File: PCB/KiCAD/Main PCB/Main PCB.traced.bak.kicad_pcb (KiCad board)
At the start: 2 copper layers, 118 x 118 mm, 130 parts, among them IC1 ADG608BRZ, IC2 ADG608BRZ, IC3 VNH7070ASTR, IC4 VNH7070ASTR, IC5 VNH7070ASTR, IC6 VNH7070ASTR, IC7 VNH7070ASTR, IC8 XB3-24Z8CM, J1 Conn_01x04, J10 Conn_01x02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

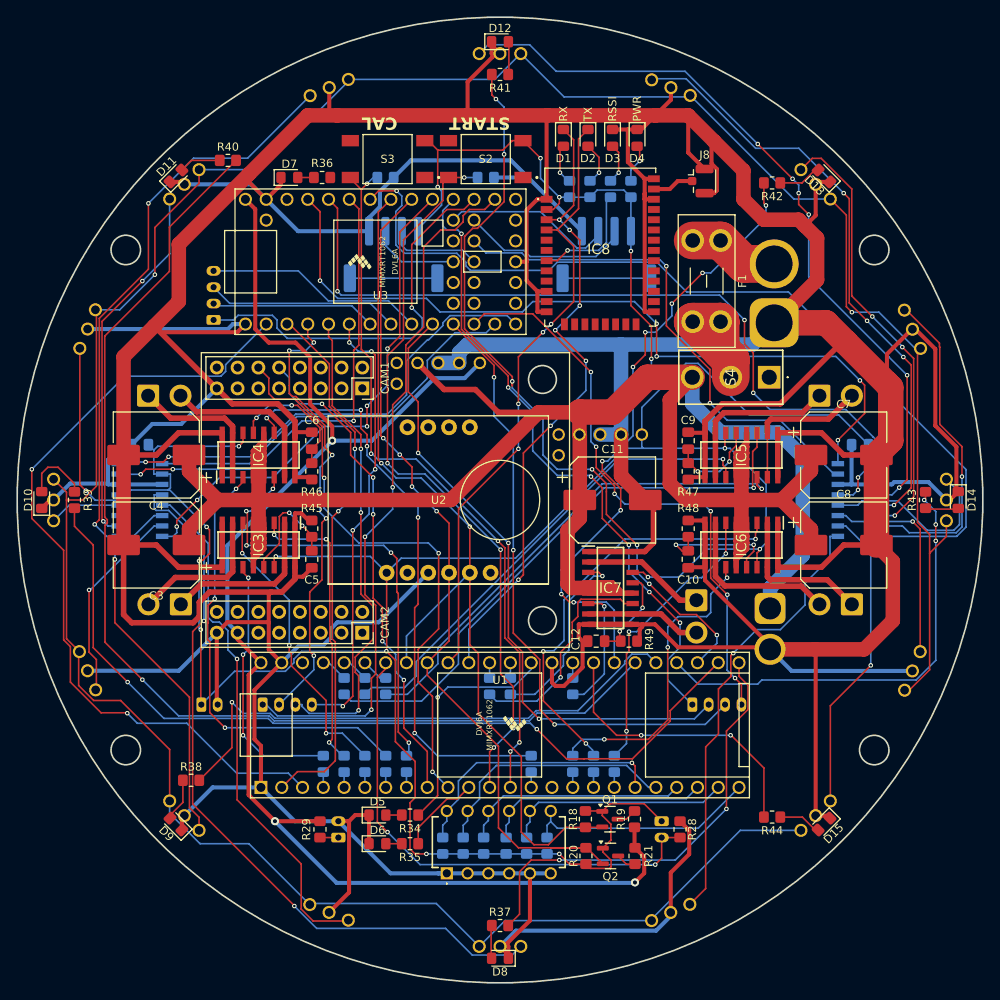
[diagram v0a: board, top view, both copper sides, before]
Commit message: Finished traces and made them curved
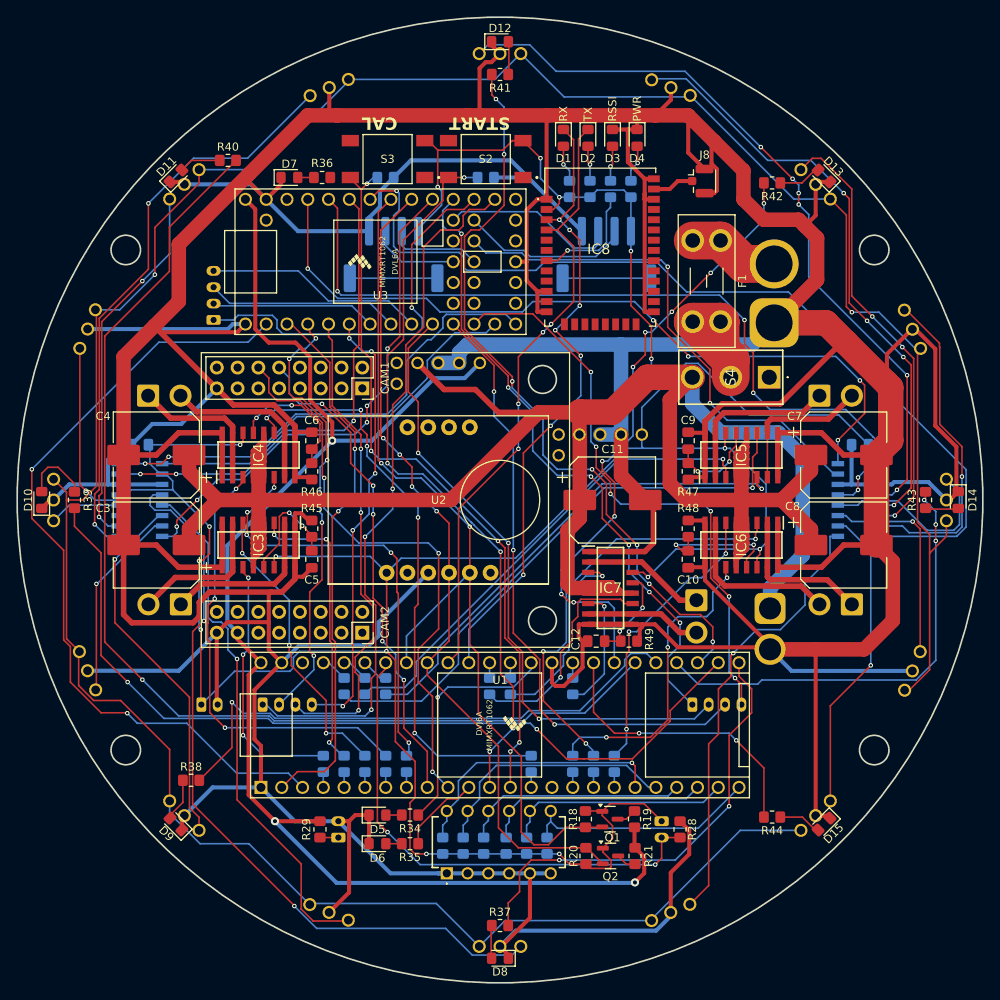
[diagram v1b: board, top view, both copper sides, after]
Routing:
- net 3V3_SDA: track 105.3 -> 101.0 mm
- net GND: track 1076.0 -> 1073.2 mm
- net TSSP_2_A1: track 96.7 -> 94.5 mm
- net IR_DIR_225: track 78.0 -> 76.4 mm
- net SPARE_SDA: track 20.6 -> 21.8 mm
- net LED_1_A0: track 55.4 -> 54.2 mm
- net IN_B_M2: track 53.6 -> 52.6 mm
- net Net-(D2-A): track 5.31 -> 4.36 mm
- net IN_A_M4: track 51.7 -> 52.6 mm
- net Net-(IC1-S4): track 24.7 -> 23.8 mm
- net TSSP_2_OUT: track 110.7 -> 111.4 mm
- net Net-(IC1-S1): track 91.0 -> 91.7 mm
- net TSSP_1_A1: track 59.2 -> 59.9 mm
- net IN_A_DRIB: track 23.4 -> 24.0 mm
- net Net-(D3-A): track 5.00 -> 4.45 mm
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
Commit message: Redone main PCB traces and started lower PCB
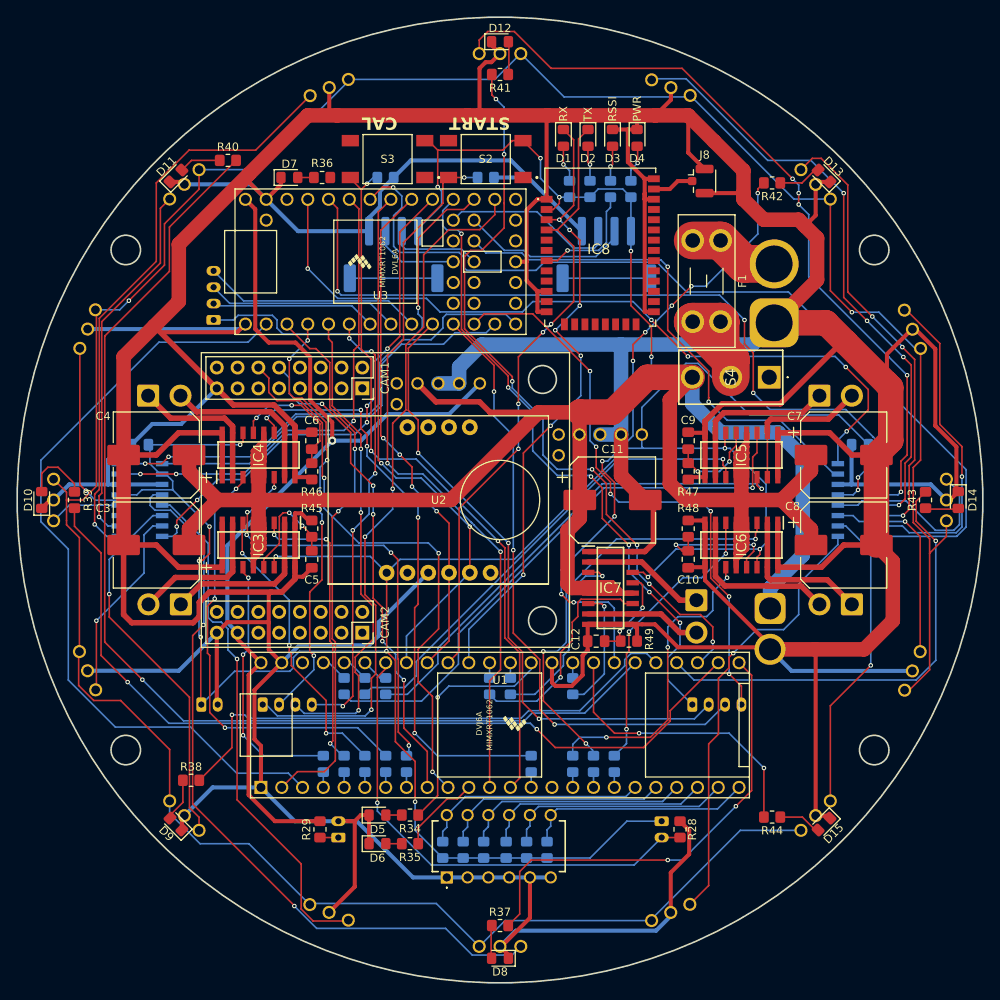
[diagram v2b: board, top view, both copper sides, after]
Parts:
- removed Q1, Q2: BSS138, Package_TO_SOT_SMD:SOT-23
- removed R18, R19, R20, R21: 10k, Resistor_SMD:R_0805_2012Metric_Pad1.20x1.40mm_HandSolder
- IR1, IR10, IR11, IR12, IR13, IR14, IR15, IR16, IR2, IR3, IR4, IR5, IR6, IR7, IR8, IR9: value TSSP4038 -> TSOP34840
- moved U5 2.50 mm to (-9.99, -5.12)
- moved R1 0.50 mm to (-7.00, 42.8)
- moved R10 0.50 mm to (0.75, 42.8)
- moved R11 0.50 mm to (3.25, 42.8)
- moved R16 0.50 mm to (5.75, 42.8)
- moved R2 0.50 mm to (-4.50, 42.8)
- moved R5 0.50 mm to (-2.00, 42.8)
- moved S1 0.50 mm to (-6.50, 46.1)
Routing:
- net +5V: track 173.5 -> 117.7 mm, vias 3 -> 1
- net 3V3_SCL: track 112.6 -> 66.9 mm
- net 3V3_SDA: track 101.0 -> 62.8 mm
- net +3V3: track 380.7 -> 367.3 mm, vias 18 -> 17
- net Net-(U1-27_A13_SCK1): track 33.0 -> 27.9 mm, vias 1 -> 0
- net GND: track 1073.2 -> 1069.8 mm
- net Net-(U1-28_RX7): track 31.1 -> 27.9 mm
- net Net-(IC2-S1): track 91.9 -> 94.6 mm, vias 6 -> 5
- net 5V_SDA: track 2.48 -> 0.00 mm
- net 5V_SCL: track 2.48 -> 0.00 mm
- net LG_RECEIVE: track 61.9 -> 59.7 mm, vias 2 -> 1
- net IR_DIR_45: track 68.0 -> 65.8 mm
- net TSSP_1_A0: track 49.0 -> 50.7 mm
- net START_BUTTON: track 90.4 -> 89.1 mm, vias 5 -> 3
- net LED_1_A0: track 54.2 -> 53.0 mm
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
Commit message: Started routing lower PCB
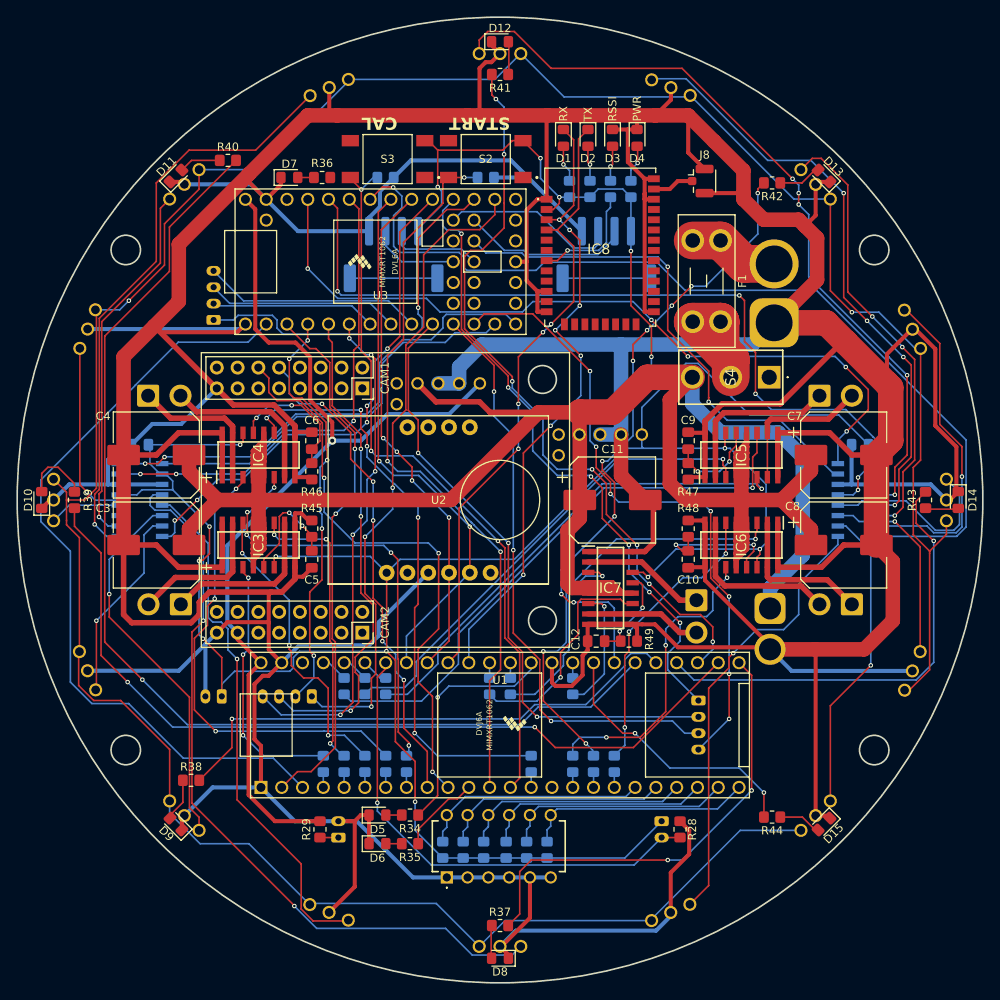
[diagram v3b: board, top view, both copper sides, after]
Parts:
- moved J1 6.08 mm to (-23.0, 24.0), turned to 180 degrees
- moved J10 2.69 mm to (-34.0, 24.0), turned to 180 degrees
- moved J3 0.90 mm to (24.2, 24.5), turned to -90 degrees
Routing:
- net LED_1_A2: track 54.2 -> 61.6 mm
- net LED_3_A2: track 71.9 -> 78.4 mm, vias 6 -> 7
- net LED_1_OUT: track 85.7 -> 79.3 mm
- net LED_3_A1: track 75.9 -> 72.1 mm
- net IR_DIR_315: track 35.7 -> 33.4 mm
- net IN_A_M2: track 53.8 -> 56.0 mm
- net TSSP_2_OUT: track 112.1 -> 114.2 mm
- net LED_3_A0: track 77.5 -> 75.5 mm
- net +3V3: track 367.3 -> 365.4 mm
- net LED_1_A0: track 53.0 -> 51.1 mm
- net GND: track 1069.8 -> 1068.2 mm
- net LED_1_A1: track 58.9 -> 60.5 mm
- net TEENSY_1_TX: track 96.7 -> 95.3 mm
- net TSSP_2_A0: track 92.8 -> 94.1 mm
- net IN_B_M1: track 35.9 -> 36.9 mm
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
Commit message: Added another switch
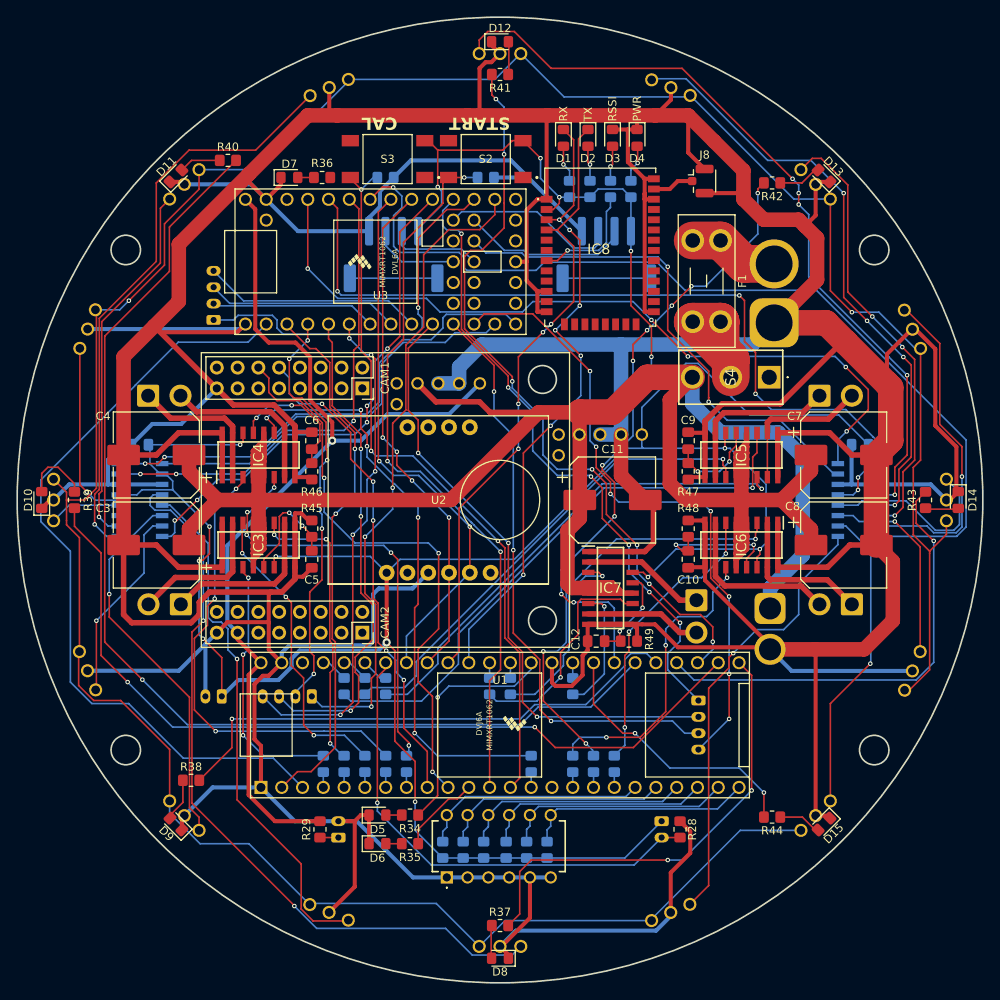
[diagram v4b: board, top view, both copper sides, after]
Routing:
- net GND: track 1068.2 -> 1071.4 mm
- net +3V3: track 365.4 -> 364.9 mm
